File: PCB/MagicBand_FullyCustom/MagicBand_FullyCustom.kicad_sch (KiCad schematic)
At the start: 20 parts, among them J2 MFRC522_Module, J3 RF_TX_DFLIFE, J4 MOSFET_DRV_IN, J5 MOSFET_DRV_OUT, J6 NeoPixel_Outer_16px, J7 NeoPixel_Inner_12px, J8 PWR_IN_5V, J9 ISP_AVR_2x3, U1 ATmega328P-P, U2 MCP1700-3302, Y1 16MHz

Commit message: Fix MOSFET driver connector footprint mismatch (JST-PH, not 2.54mm header)
Component-selection audit caught this: Adafruit MOSFET Driver (PID 5648)
uses a single 3-pin STEMMA JST-PH connector at 2mm pitch (V+/GND/In
together, confirmed against Adafruit's own pinout docs), not a generic
2.54mm/0.1" pin header. The two aren't physically compatible -- the real
cable would not have mated with what was drawn. Swapped J4's footprint to
JST_PH_B3B-PH-K_1x03_P2.00mm_Vertical, confirmed against KiCad's official
footprint repo. ERC re-run clean, no regression (0 errors, same 206
warnings).

Lipo Rider Plus's 5V output connector (J8) is flagged as still unverified
-- its 5V rail appears to route through a USB Type-A port rather than a
simple header pin, per available documentation; needs a direct look at
Seeed's pin diagram before locking that footprint in.

Co-Authored-By: Claude Sonnet 5 <noreply@anthropic.com>
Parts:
- C5: footprint Capacitor_THT:C_Disc_D3.0mm_W2.5mm_P2.50mm -> Capacitor_THT:C_Disc_D5.0mm_W2.5mm_P5.00mm
- J4: footprint Connector_PinHeader_2.54mm:PinHeader_1x03_P2.54mm_Vertical -> Connector_JST:JST_PH_B3B-PH-K_1x03_P2.00mm_Vertical
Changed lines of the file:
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@@
 			(effects (font (size 1.27 1.27)))
 		)
-		(property "Footprint" "Capacitor_THT:C_Disc_D3.0mm_W2.5mm_P2.50mm"
+		(property "Footprint" "Capacitor_THT:C_Disc_D5.0mm_W2.5mm_P5.00mm"
 			(at 170 100 0)
 			(effects (font (size 1.27 1.27)) (hide yes))
@@
 			(effects (font (size 1.27 1.27)))
 		)
-		(property "Footprint" "Connector_PinHeader_2.54mm:PinHeader_1x03_P2.54mm_Vertical"
+		(property "Footprint" "Connector_JST:JST_PH_B3B-PH-K_1x03_P2.00mm_Vertical"
 			(at 250 70 0)
 			(effects (font (size 1.27 1.27)) (hide yes))

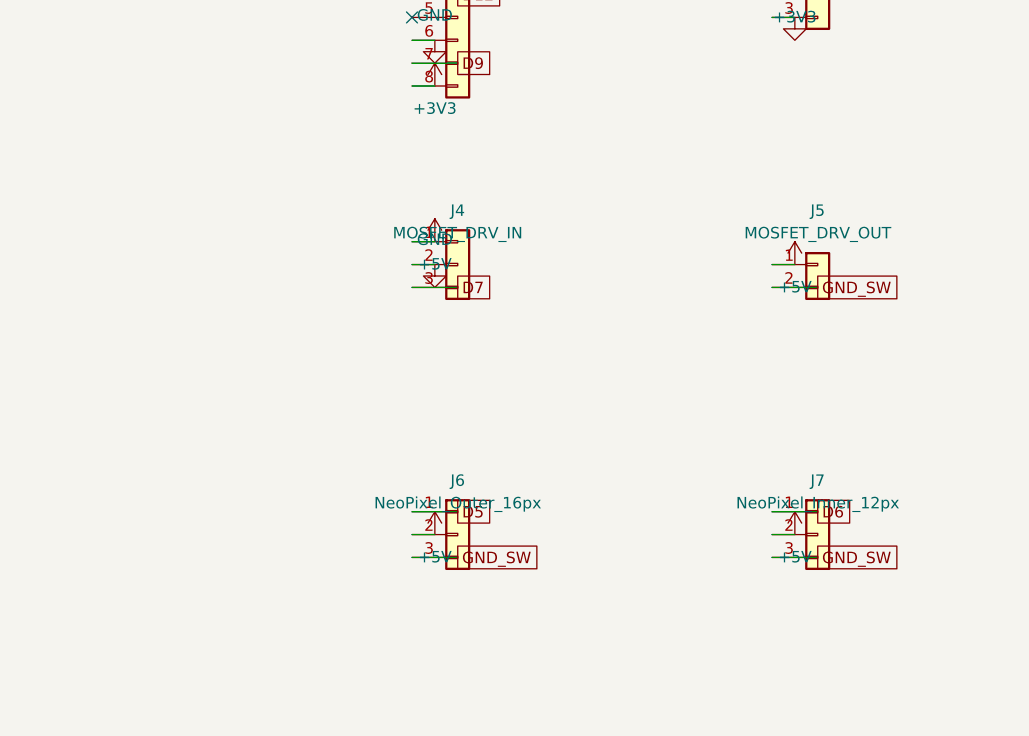
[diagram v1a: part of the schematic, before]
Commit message: Integrate MOSFET switch circuit directly into v2 schematic
Replaces the external Adafruit MOSFET driver module (J4/J5, JST-PH
connector) with an on-board MOSFET switch: Q1 (N-channel logic-level
MOSFET, e.g. AO3400A/SOT-23), R2 (100R gate series resistor), R3 (10k
gate pull-down for a defined-off startup state before firmware drives
D7). Same low-side-switching topology as before -- verified via the
exported netlist, not just ERC, that NeoPixel headers J6/J7 still tie to
GND_SW correctly through Q1's drain.

Deliberate scope call, not a mistake fix: unlike the RFID/RF modules
(real antenna engineering, stay external by design), a MOSFET switch is
basic circuit design worth integrating directly -- removes a module and
connector from the BOM.

ERC clean: 0 errors, 208 warnings (was 206, same cosmetic categories).
Prior PCB layout attempt removed as stale (routed against the old J4/J5
netlist) -- needs a fresh layout pass against this schematic.

Co-Authored-By: Claude Sonnet 5 <noreply@anthropic.com>
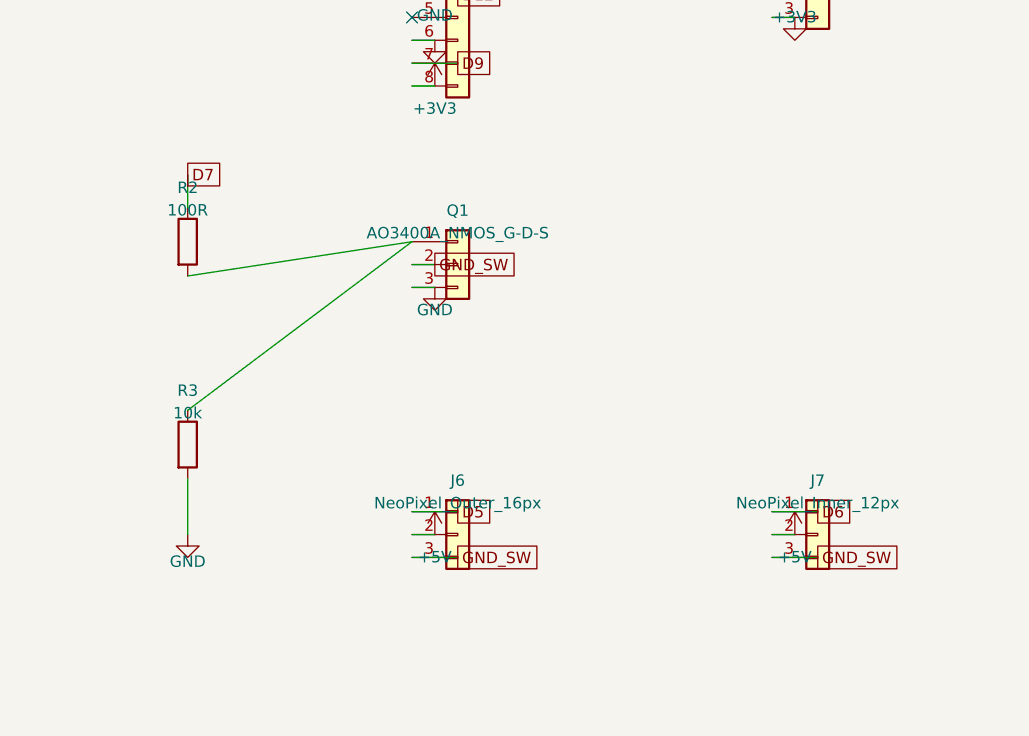
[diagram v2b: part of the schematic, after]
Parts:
- removed J4: MOSFET_DRV_IN, Connector_JST:JST_PH_B3B-PH-K_1x03_P2.00mm_Vertical, symbol Connector_Generic:Conn_01x03
- removed J5: MOSFET_DRV_OUT, Connector_PinHeader_2.54mm:PinHeader_1x02_P2.54mm_Vertical, symbol Connector_Generic:Conn_01x02
- added Q1: AO3400A_NMOS_G-D-S, Package_TO_SOT_SMD:SOT-23, symbol Connector_Generic:Conn_01x03
- added R2: 100R, Resistor_THT:R_Axial_DIN0207_L6.3mm_D2.5mm_P10.16mm_Horizontal, symbol Device:R
- added R3: 10k, Resistor_THT:R_Axial_DIN0207_L6.3mm_D2.5mm_P10.16mm_Horizontal, symbol Device:R
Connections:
- net D7: now also R2.1
- net GND: now also Q1.3 (Pin_3), R3.2
- net GND_SW: now also Q1.2 (Pin_2)
- new net: Q1.1 (Pin_1), R2.2, R3.1
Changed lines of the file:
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@@
 		(on_board yes)
 		(dnp no)
-		(property "Reference" "J4"
+		(property "Reference" "Q1"
 			(at 250 64 0)
 			(effects (font (size 1.27 1.27)))
 		)
-		(property "Value" "MOSFET_DRV_IN"
+		(property "Value" "AO3400A_NMOS_G-D-S"
 			(at 250 66.5 0)
 			(effects (font (size 1.27 1.27)))
 		)
-		(property "Footprint" "Connector_JST:JST_PH_B3B-PH-K_1x03_P2.00mm_Vertical"
+		(property "Footprint" "Package_TO_SOT_SMD:SOT-23"
 			(at 250 70 0)
 			(effects (font (size 1.27 1.27)) (hide yes))
@@
 			(project "MagicBand_FullyCustom"
 				(path "/bcfef247-dfd6-4ae3-b42f-2bc22ccfcf8a"
-					(reference "J4")
-					(unit 1)
-				)
-			)
-		)
-	)
-	(wire
-		(pts (xy 244.92 67.46) (xy 247.46 67.46))
-		(stroke (width 0) (type default))
-	)
-	(symbol
-		(lib_id "power:+5V")
-		(at 247.46 67.46 0)
-		(unit 1)
-		(exclude_from_sim no)
-		(in_bom yes)
-		(on_board yes)
-		(dnp no)
-		(property "Reference" "#PWR0b3b"
-			(at 247.46 63.959999999999994 0)
-			(effects (font (size 1.27 1.27)) (hide yes))
-		)
-		(property "Value" "+5V"
-			(at 247.46 69.96 0)
+					(reference "Q1")
+					(unit 1)
+				)
+			)
+		)
+	)
+	(wire
+		(pts (xy 244.92 70.0) (xy 247.46 70.0))
+		(stroke (width 0) (type default))
+	)
+	(global_label "GND_SW"
+		(shape passive)
+		(at 247.46 70.0 0)
+		(fields_autoplaced yes)
+		(effects (font (size 1.27 1.27)) (justify left))
+	)
+	(wire
+		(pts (xy 244.92 72.54) (xy 247.46 72.54))
+		(stroke (width 0) (type default))
+	)
+	(symbol
+		(lib_id "power:GND")
+		(at 247.46 72.54 0)
+		(unit 1)
+		(exclude_from_sim no)
+		(in_bom yes)
+		(on_board yes)
+		(dnp no)
+		(property "Reference" "#PWRQ1S"
+			(at 247.46 69.04 0)
+			(effects (font (size 1.27 1.27)) (hide yes))
+		)
+		(property "Value" "GND"
+			(at 247.46 75.04 0)
 			(effects (font (size 1.27 1.27)))
 		)
 		(property "Footprint" ""
-			(at 247.46 67.46 0)
-			(effects (font (size 1.27 1.27)) (hide yes))
-		)
-		(property "Datasheet" ""
-			(at 247.46 67.46 0)
-			(effects (font (size 1.27 1.27)) (hide yes))
-		)
-		(pin "1")
-		(instances
-			(project "MagicBand_FullyCustom"
-				(path "/bcfef247-dfd6-4ae3-b42f-2bc22ccfcf8a"
-					(reference "#PWR0b3b")
-					(unit 1)
-				)
-			)
-		)
-	)
-	(wire
-		(pts (xy 244.92 70.0) (xy 247.46 70.0))
-		(stroke (width 0) (type default))
-	)
-	(symbol
-		(lib_id "power:GND")
-		(at 247.46 70.0 0)
-		(unit 1)
-		(exclude_from_sim no)
-		(in_bom yes)
-		(on_board yes)
-		(dnp no)
-		(property "Reference" "#PWRbc69"
-			(at 247.46 66.5 0)
-			(effects (font (size 1.27 1.27)) (hide yes))
-		)
-		(property "Value" "GND"
-			(at 247.46 67.23 0)
-			(effects (font (size 1.27 1.27)))
-		)
-		(property "Footprint" ""
-			(at 247.46 70.0 0)
-			(effects (font (size 1.27 1.27)) (hide yes))
-		)
-		(property "Datasheet" ""
-			(at 247.46 70.0 0)
-			(effects (font (size 1.27 1.27)) (hide yes))
-		)
-		(pin "1")
-		(instances
-			(project "MagicBand_FullyCustom"
-				(path "/bcfef247-dfd6-4ae3-b42f-2bc22ccfcf8a"
-					(reference "#PWRbc69")
-					(unit 1)
-				)
-			)
-		)
-	)
-	(wire
-		(pts (xy 244.92 72.54) (xy 250.0 72.54))
+			(at 247.46 72.54 0)
+			(effects (font (size 1.27 1.27)) (hide yes))
+		)
+		(property "Datasheet" ""
+			(at 247.46 72.54 0)
+			(effects (font (size 1.27 1.27)) (hide yes))
+		)
+		(pin "1")
+		(instances
+			(project "MagicBand_FullyCustom"
+				(path "/bcfef247-dfd6-4ae3-b42f-2bc22ccfcf8a"
+					(reference "#PWRQ1S")
+					(unit 1)
+				)
+			)
+		)
+	)
+	(wire
+		(pts (xy 220 71.27) (xy 244.92 67.46))
+		(stroke (width 0) (type default))
+	)
+	(symbol
+		(lib_id "Device:R")
+		(at 220 67.46 0)
+		(unit 1)
+		(exclude_from_sim no)
+		(in_bom yes)
+		(on_board yes)
+		(dnp no)
+		(property "Reference" "R2"
+			(at 220 61.46 0)
+			(effects (font (size 1.27 1.27)))
+		)
+		(property "Value" "100R"
+			(at 220 63.96 0)
+			(effects (font (size 1.27 1.27)))
+		)
+		(property "Footprint" "Resistor_THT:R_Axial_DIN0207_L6.3mm_D2.5mm_P10.16mm_Horizontal"
+			(at 220 67.46 0)
+			(effects (font (size 1.27 1.27)) (hide yes))
+		)
+		(property "Datasheet" ""
+			(at 220 67.46 0)
+			(effects (font (size 1.27 1.27)) (hide yes))
+		)
+		(pin "1")
+		(pin "2")
+		(instances
+			(project "MagicBand_FullyCustom"
+				(path "/bcfef247-dfd6-4ae3-b42f-2bc22ccfcf8a"
+					(reference "R2")
+					(unit 1)
+				)
+			)
+		)
+	)
+	(wire
+		(pts (xy 220 63.65) (xy 220 60.0))
 		(stroke (width 0) (type default))
 	)
 	(global_label "D7"
 		(shape passive)
-		(at 250.0 72.54 0)
+		(at 220 60.0 0)
 		(fields_autoplaced yes)
 		(effects (font (size 1.27 1.27)) (justify left))
 	)
-	(symbol
-		(lib_id "Connector_Generic:Conn_01x02")
-		(at 290 70 0)
-		(unit 1)
-		(exclude_from_sim no)
-		(in_bom yes)
-		(on_board yes)
-		(dnp no)
-		(property "Reference" "J5"
-			(at 290 64 0)
-			(effects (font (size 1.27 1.27)))
-		)
-		(property "Value" "MOSFET_DRV_OUT"
-			(at 290 66.5 0)
-			(effects (font (size 1.27 1.27)))
-		)
-		(property "Footprint" "Connector_PinHeader_2.54mm:PinHeader_1x02_P2.54mm_Vertical"
-			(at 290 70 0)
-			(effects (font (size 1.27 1.27)) (hide yes))
-		)
-		(property "Datasheet" ""
-			(at 290 70 0)
+	(wire
+		(pts (xy 220 93.81) (xy 220 100.0))
+		(stroke (width 0) (type default))
+	)
+	(symbol
+		(lib_id "power:GND")
+		(at 220 100.0 0)
+		(unit 1)
+		(exclude_from_sim no)
+		(in_bom yes)
+		(on_board yes)
+		(dnp no)
+		(property "Reference" "#PWRR3"
+			(at 220 96.5 0)
+			(effects (font (size 1.27 1.27)) (hide yes))
+		)
+		(property "Value" "GND"
+			(at 220 103.0 0)
+			(effects (font (size 1.27 1.27)))
+		)
+		(property "Footprint" ""
+			(at 220 100.0 0)
+			(effects (font (size 1.27 1.27)) (hide yes))
+		)
+		(property "Datasheet" ""
+			(at 220 100.0 0)
+			(effects (font (size 1.27 1.27)) (hide yes))
+		)
+		(pin "1")
+		(instances
+			(project "MagicBand_FullyCustom"
+				(path "/bcfef247-dfd6-4ae3-b42f-2bc22ccfcf8a"
+					(reference "#PWRR3")
+					(unit 1)
+				)
+			)
+		)
+	)
+	(wire
+		(pts (xy 220 86.19) (xy 244.92 67.46))
+		(stroke (width 0) (type default))
+	)
+	(symbol
+		(lib_id "Device:R")
+		(at 220 90.0 0)
+		(unit 1)
+		(exclude_from_sim no)
+		(in_bom yes)
+		(on_board yes)
+		(dnp no)
+		(property "Reference" "R3"
+			(at 220 84.0 0)
+			(effects (font (size 1.27 1.27)))
+		)
+		(property "Value" "10k"
+			(at 220 86.5 0)
+			(effects (font (size 1.27 1.27)))
+		)
+		(property "Footprint" "Resistor_THT:R_Axial_DIN0207_L6.3mm_D2.5mm_P10.16mm_Horizontal"
+			(at 220 90.0 0)
+			(effects (font (size 1.27 1.27)) (hide yes))
+		)
+		(property "Datasheet" ""
+			(at 220 90.0 0)
 			(effects (font (size 1.27 1.27)) (hide yes))
 		)
@@
 			(project "MagicBand_FullyCustom"
 				(path "/bcfef247-dfd6-4ae3-b42f-2bc22ccfcf8a"
-					(reference "J5")
-					(unit 1)
-				)
-			)
-		)
-	)
-	(wire
-		(pts (xy 284.92 70.0) (xy 287.46 70.0))
-		(stroke (width 0) (type default))
-	)
-	(symbol
-		(lib_id "power:+5V")
-		(at 287.46 70.0 0)
-		(unit 1)
-		(exclude_from_sim no)
-		(in_bom yes)
-		(on_board yes)
-		(dnp no)
-		(property "Reference" "#PWR178f"
-			(at 287.46 66.5 0)
-			(effects (font (size 1.27 1.27)) (hide yes))
-		)
-		(property "Value" "+5V"
-			(at 287.46 72.5 0)
-			(effects (font (size 1.27 1.27)))
-		)
-		(property "Footprint" ""
-			(at 287.46 70.0 0)
-			(effects (font (size 1.27 1.27)) (hide yes))
-		)
-		(property "Datasheet" ""
-			(at 287.46 70.0 0)
-			(effects (font (size 1.27 1.27)) (hide yes))
-		)
-		(pin "1")
-		(instances
-			(project "MagicBand_FullyCustom"
-				(path "/bcfef247-dfd6-4ae3-b42f-2bc22ccfcf8a"
-					(reference "#PWR178f")
-					(unit 1)
-				)
-			)
-		)
-	)
-	(wire
-		(pts (xy 284.92 72.54) (xy 290.0 72.54))
-		(stroke (width 0) (type default))
-	)
-	(global_label "GND_SW"
-		(shape passive)
-		(at 290.0 72.54 0)
-		(fields_autoplaced yes)
-		(effects (font (size 1.27 1.27)) (justify left))
-	)
-	(symbol
+					(reference "R3")
+					(unit 1)
+				)
+			)
+		)
+	)
+	(symbol

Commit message: MFRC522 as a stacking header, not loose wires
J2's footprint changed from a male pin header to a female socket strip
(PinSocket_1x08_P2.54mm_Vertical) so the MFRC522 breakout's own header
pins plug directly into the custom board -- shield-style stacking instead
of jumper wires. Addresses the "two loose boards to mount inside the
ornament" problem mechanically. Full chip-level MFRC522 integration was
considered and rejected (real antenna-tuning engineering, likely needs
re-tuning once mounted -- not worth the risk this project has been
explicitly trying to avoid). ERC re-run clean, no regression.

Co-Authored-By: Claude Sonnet 5 <noreply@anthropic.com>
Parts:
- J2: footprint PinHeader_2.54mm:PinHeader_1x08_P2.54mm_Vertical -> Connector_PinSocket_2.54mm:PinSocket_1x08_P2.54mm_Vertical
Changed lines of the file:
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@@
 			(effects (font (size 1.27 1.27)))
 		)
-		(property "Footprint" "PinHeader_2.54mm:PinHeader_1x08_P2.54mm_Vertical"
+		(property "Footprint" "Connector_PinSocket_2.54mm:PinSocket_1x08_P2.54mm_Vertical"
 			(at 250 40 0)
 			(effects (font (size 1.27 1.27)) (hide yes))
